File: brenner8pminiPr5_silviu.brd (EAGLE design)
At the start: 82.5 x 43 mm, 39 parts, among them IC1 PIC18F2550SP, Q1 20 MHz, Q2 BC338-25, Q3 BC338-25, Q4 BC328-25, Q5 BC328-25, Q6 BF959, X2 USB-B-H

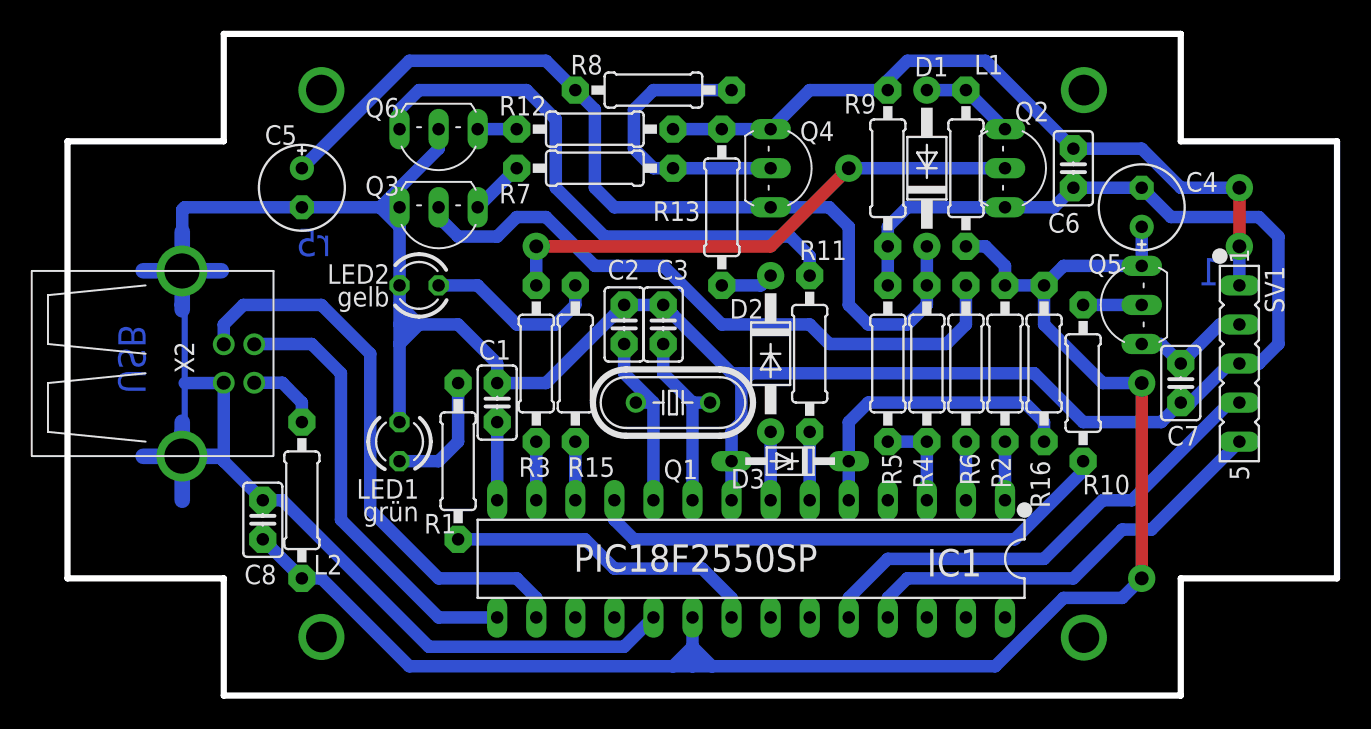
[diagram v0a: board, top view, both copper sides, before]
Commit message: Fixed DRC clearances and pad shapes
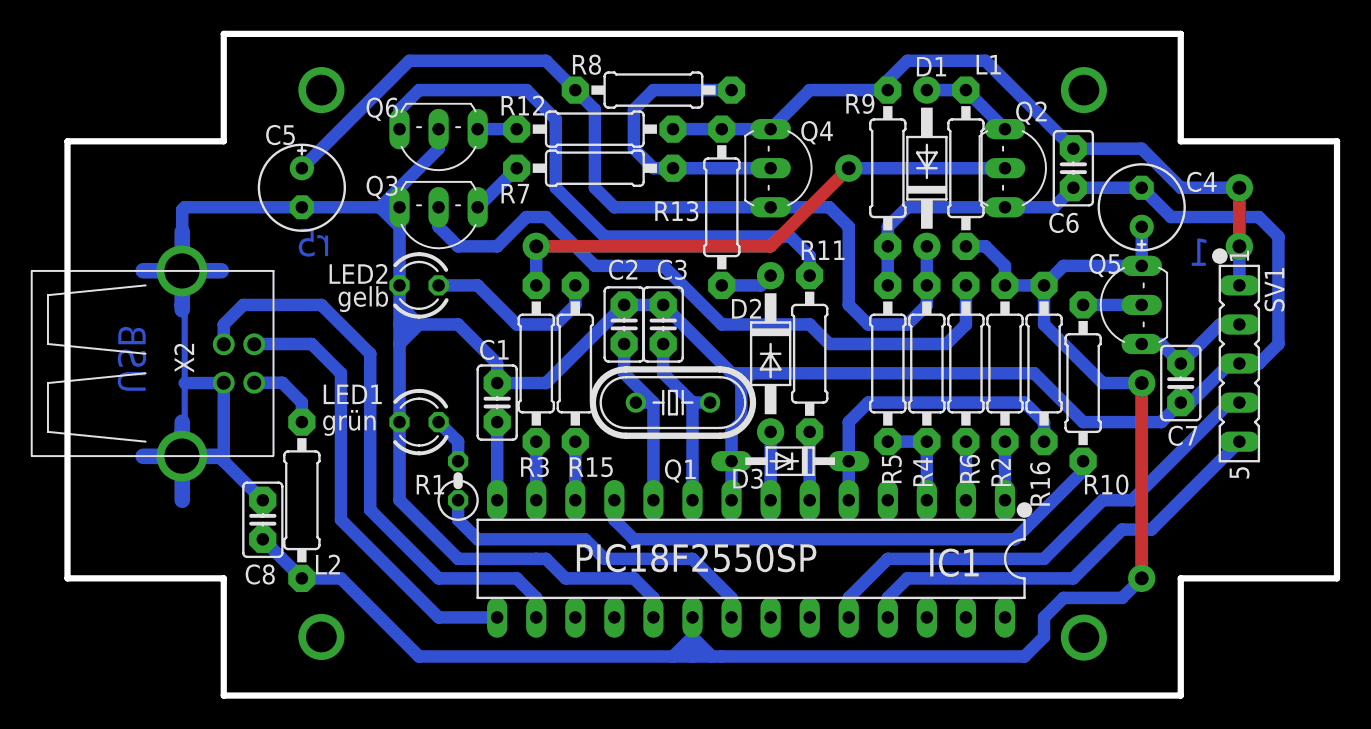
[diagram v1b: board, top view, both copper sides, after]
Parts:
- R1: device rcl:0207/10 -> rcl:0207/2V
- moved LED1 1.80 mm to (22.9, 16.5), turned to 180 degrees
- moved R1 1.27 mm to (25.4, 12.7)
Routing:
- net N$4: track 8.15 -> 3.07 mm
- net VSS: track 231.5 -> 226.8 mm
- net N$16: track 20.6 -> 22.4 mm
- net N$21: track 42.5 -> 43.4 mm

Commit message: Added silkscreen labels. Final DRC error fixes
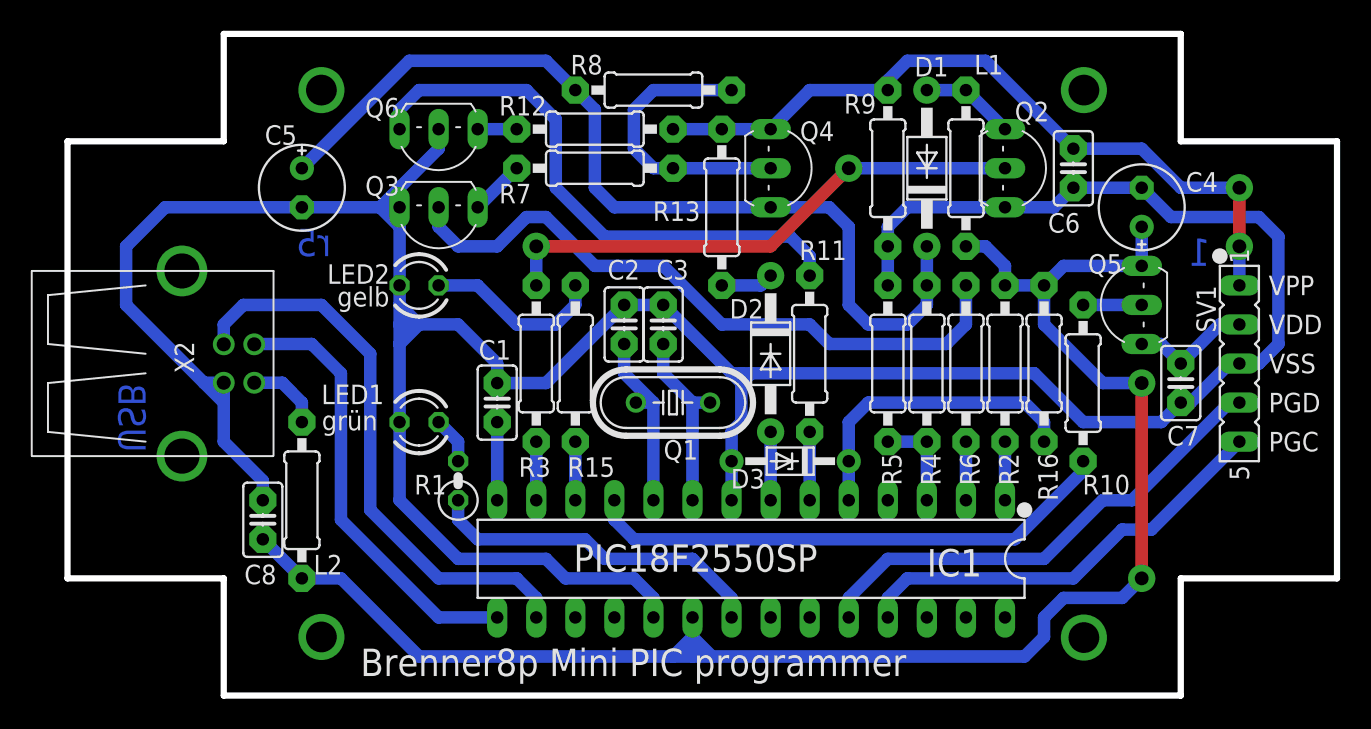
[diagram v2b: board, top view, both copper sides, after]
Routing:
- net VSS: track 226.8 -> 210.1 mm
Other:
- board text added: "Brenner8p Mini PIC programmer"
- board text added: "PGC"
- board text added: "PGD"
- board text added: "VDD"
- board text added: "VPP"
- board text added: "VSS"
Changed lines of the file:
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@@
 <wire x1="82.55" y1="34.77" x2="72.39" y2="34.77" width="0.4064" layer="20"/>
 <wire x1="82.55" y1="6.35" x2="72.39" y2="6.35" width="0.4064" layer="20"/>
-<text x="5.08" y="22.86" size="1.778" layer="16" font="vector" ratio="15" rot="MR270">USB</text>
+<text x="5.08" y="19.05" size="1.778" layer="16" font="vector" ratio="15" rot="MR270">USB</text>
 <text x="17.145" y="27.305" size="1.778" layer="16" font="vector" ratio="15" rot="MR0">r5</text>
 <text x="74.295" y="26.67" size="1.778" layer="16" font="vector" ratio="15" rot="MR0">1</text>
 <circle x="74.93" y="27.305" radius="0.508" width="0" layer="21"/>
 <circle x="62.23" y="10.795" radius="0.508" width="0" layer="21"/>
+<text x="19.05" y="0" size="1.778" layer="21">Brenner8p Mini PIC programmer</text>
+<text x="78.105" y="24.765" size="1.27" layer="21" ratio="10">VPP</text>
+<text x="78.105" y="22.225" size="1.27" layer="21" ratio="10">VDD</text>
+<text x="78.105" y="19.685" size="1.27" layer="21" ratio="10">VSS</text>
+<text x="78.105" y="17.145" size="1.27" layer="21" ratio="10">PGD</text>
+<text x="78.105" y="14.605" size="1.27" layer="21" ratio="10">PGC</text>
 </plain>
 <attributes>
@@
 </element>
 <element name="Q1" library="crystal" package="HC49/S" value="20 MHz" x="39.37" y="17.78" smashed="yes">
-<attribute name="NAME" x="38.7604" y="12.8016" size="1.27" layer="25" ratio="10"/>
+<attribute name="NAME" x="38.7604" y="14.0716" size="1.27" layer="25" ratio="10"/>
 <attribute name="VALUE" x="36.83" y="13.7922" size="1.27" layer="27" ratio="10"/>
 </element>
@@
 </element>
 <element name="R2" library="rcl" package="0207/10" value="10 k" x="60.96" y="20.32" smashed="yes" rot="R90">
-<attribute name="NAME" x="61.341" y="12.192" size="1.27" layer="25" ratio="10" rot="R90"/>
+<attribute name="NAME" x="60.579" y="14.478" size="1.27" layer="25" ratio="10" rot="R270"/>
 <attribute name="VALUE" x="61.595" y="18.0594" size="1.27" layer="27" ratio="10" rot="R90"/>
 </element>
@@
 </element>
 <element name="R4" library="rcl" package="0207/10" value="4k7" x="55.88" y="20.32" smashed="yes" rot="R90">
-<attribute name="NAME" x="56.261" y="12.192" size="1.27" layer="25" ratio="10" rot="R90"/>
+<attribute name="NAME" x="55.499" y="14.478" size="1.27" layer="25" ratio="10" rot="R270"/>
 <attribute name="VALUE" x="56.515" y="19.3294" size="1.27" layer="27" ratio="10" rot="R90"/>
 </element>
@@
 <attribute name="VALUE" x="11.049" y="8.001" size="1.27" layer="27" ratio="10" rot="R90"/>
 </element>
-<element name="SV1" library="con-lsta" package="FE05-1" value="ICSP" x="76.2" y="20.32" rot="R270"/>
+<element name="SV1" library="con-lsta" package="FE05-1" value="ICSP" x="76.2" y="20.32" smashed="yes" rot="R270">
+<attribute name="NAME" x="73.406" y="25.4" size="1.27" layer="25" ratio="10" rot="R270"/>
+<attribute name="VALUE" x="77.851" y="20.32" size="1.27" layer="27" ratio="10" rot="R270"/>
+</element>
 <element name="R15" library="rcl" package="0207/10" value="1 k" x="33.02" y="20.32" smashed="yes" rot="R270">
 <attribute name="NAME" x="32.512" y="12.954" size="1.27" layer="25" ratio="10"/>
@@
 </element>
 <element name="R16" library="rcl" package="0207/10" value="330" x="63.5" y="20.32" smashed="yes" rot="R90">
-<attribute name="NAME" x="63.881" y="10.922" size="1.27" layer="25" ratio="10" rot="R90"/>
+<attribute name="NAME" x="63.119" y="14.478" size="1.27" layer="25" ratio="10" rot="R270"/>
 <attribute name="VALUE" x="64.135" y="18.6944" size="1.27" layer="27" ratio="10" rot="R90"/>
 </element>
@@
 <wire x1="68.58" y1="5.08" x2="69.85" y2="6.35" width="0.8128" layer="16"/>
 <wire x1="40.64" y1="1.27" x2="41.91" y2="1.27" width="0.8128" layer="16"/>
-<wire x1="41.91" y1="1.27" x2="42.545" y2="1.27" width="0.8128" layer="16"/>
-<wire x1="42.545" y1="1.27" x2="62.23" y2="1.27" width="0.8128" layer="16"/>
+<wire x1="41.91" y1="1.27" x2="62.23" y2="1.27" width="0.8128" layer="16"/>
 <wire x1="62.23" y1="1.27" x2="63.5" y2="2.54" width="0.8128" layer="16"/>
 <wire x1="63.5" y1="2.54" x2="63.5" y2="3.81" width="0.8128" layer="16"/>
@@
 <wire x1="67.31" y1="19.05" x2="63.5" y2="22.86" width="0.8128" layer="16"/>
 <wire x1="63.5" y1="22.86" x2="63.5" y2="25.4" width="0.8128" layer="16"/>
-<wire x1="40.64" y1="1.27" x2="40.64" y2="1.905" width="0.8128" layer="16"/>
-<wire x1="40.64" y1="1.905" x2="40.64" y2="2.54" width="0.8128" layer="16"/>
+<wire x1="40.64" y1="1.27" x2="40.64" y2="2.54" width="0.8128" layer="16"/>
 <wire x1="40.64" y1="2.54" x2="40.64" y2="3.81" width="0.8128" layer="16"/>
 <wire x1="22.86" y1="1.27" x2="39.37" y2="1.27" width="0.8128" layer="16"/>
@@
 <wire x1="77.47" y1="29.845" x2="71.755" y2="29.845" width="0.8128" layer="16"/>
 <wire x1="27.94" y1="19.05" x2="31.115" y2="19.05" width="0.8128" layer="16"/>
-<wire x1="10.16" y1="19.05" x2="10.16" y2="19.07" width="0.8128" layer="16"/>
-<wire x1="10.16" y1="13.97" x2="12.7" y2="11.43" width="0.8128" layer="16"/>
-<wire x1="10.16" y1="19.05" x2="10.16" y2="13.97" width="0.8128" layer="16"/>
-<wire x1="7.62" y1="19.05" x2="10.16" y2="19.05" width="0.8128" layer="16"/>
-<wire x1="7.62" y1="30.48" x2="15.24" y2="30.48" width="0.8128" layer="16"/>
 <wire x1="15.24" y1="30.48" x2="20.32" y2="30.48" width="0.8128" layer="16"/>
 <wire x1="20.32" y1="30.48" x2="21.59" y2="30.48" width="0.8128" layer="16"/>
-<wire x1="7.4612" y1="24.13" x2="7.4612" y2="23.8125" width="1.016" layer="16"/>
-<wire x1="7.4612" y1="24.13" x2="7.4612" y2="28.8925" width="1.016" layer="16"/>
-<wire x1="7.62" y1="26.3525" x2="4.9213" y2="26.3525" width="1.016" layer="16"/>
-<wire x1="7.62" y1="26.3525" x2="10.0013" y2="26.3525" width="1.016" layer="16"/>
-<wire x1="10.0013" y1="14.2875" x2="4.9213" y2="14.2875" width="1.016" layer="16"/>
-<wire x1="7.4612" y1="11.43" x2="7.4612" y2="15.875" width="1.016" layer="16"/>
-<wire x1="7.4612" y1="15.875" x2="7.4612" y2="16.51" width="1.016" layer="16"/>
 <wire x1="43.18" y1="19.685" x2="43.815" y2="19.685" width="0.8128" layer="16"/>
 <wire x1="43.815" y1="19.685" x2="44.45" y2="19.685" width="0.8128" layer="16"/>
@@
 <wire x1="71.12" y1="16.51" x2="72.39" y2="17.78" width="0.8128" layer="16"/>
 <wire x1="36.195" y1="24.13" x2="38.735" y2="24.13" width="0.8128" layer="16"/>
-<wire x1="35.56" y1="23.495" x2="36.195" y2="24.13" width="0.8128" layer="16"/>
-<wire x1="31.115" y1="19.05" x2="35.56" y2="23.495" width="0.8128" layer="16"/>
-<wire x1="38.735" y1="24.13" x2="39.37" y2="23.495" width="0.8128" layer="16"/>
-<wire x1="39.37" y1="23.495" x2="43.18" y2="19.685" width="0.8128" layer="16"/>
-<wire x1="7.4612" y1="28.8925" x2="7.4612" y2="30.3212" width="0.8128" layer="16"/>
-<wire x1="7.4612" y1="30.3212" x2="7.62" y2="30.48" width="0.8128" layer="16"/>
-<wire x1="10.0013" y1="14.1287" x2="10.0013" y2="14.2875" width="0.8128" layer="16"/>
-<wire x1="10.16" y1="13.97" x2="10.0013" y2="14.1287" width="0.8128" layer="16"/>
-<wire x1="7.62" y1="24.13" x2="7.4612" y2="24.13" width="0.4064" layer="16"/>
-<wire x1="7.62" y1="19.05" x2="7.62" y2="24.13" width="0.4064" layer="16"/>
-<wire x1="7.62" y1="24.13" x2="7.62" y2="26.3525" width="0.4064" layer="16"/>
-<wire x1="7.4612" y1="15.875" x2="7.62" y2="15.875" width="0.4064" layer="16"/>
-<wire x1="7.62" y1="15.875" x2="7.62" y2="19.05" width="0.4064" layer="16"/>
+<wire x1="31.115" y1="19.05" x2="36.195" y2="24.13" width="0.8128" layer="16"/>
+<wire x1="38.735" y1="24.13" x2="43.18" y2="19.685" width="0.8128" layer="16"/>
 <wire x1="21.59" y1="31.75" x2="24.13" y2="34.29" width="0.8128" layer="16"/>
 <wire x1="21.59" y1="30.48" x2="21.59" y2="31.75" width="0.8128" layer="16"/>
@@
 <wire x1="36.83" y1="6.35" x2="32.385" y2="6.35" width="0.8128" layer="16"/>
 <wire x1="32.385" y1="6.35" x2="31.115" y2="7.62" width="0.8128" layer="16"/>
-<wire x1="31.115" y1="7.62" x2="30.48" y2="7.62" width="0.8128" layer="16"/>
-<wire x1="30.48" y1="7.62" x2="25.4" y2="7.62" width="0.8128" layer="16"/>
+<wire x1="31.115" y1="7.62" x2="25.4" y2="7.62" width="0.8128" layer="16"/>
 <wire x1="25.4" y1="7.62" x2="21.59" y2="11.43" width="0.8128" layer="16"/>
 <wire x1="21.59" y1="11.43" x2="21.59" y2="16.51" width="0.8128" layer="16"/>
+<wire x1="12.7" y1="11.43" x2="12.7" y2="12.7" width="0.8128" layer="16"/>
+<wire x1="12.7" y1="12.7" x2="10.16" y2="15.24" width="0.8128" layer="16"/>
+<wire x1="10.16" y1="19.07" x2="8.87" y2="19.07" width="0.8128" layer="16"/>
+<wire x1="8.87" y1="19.07" x2="3.81" y2="24.13" width="0.8128" layer="16"/>
+<wire x1="3.81" y1="24.13" x2="3.81" y2="27.94" width="0.8128" layer="16"/>
+<wire x1="3.81" y1="27.94" x2="6.35" y2="30.48" width="0.8128" layer="16"/>
+<wire x1="6.35" y1="30.48" x2="15.24" y2="30.48" width="0.8128" layer="16"/>
+<wire x1="10.16" y1="19.07" x2="10.16" y2="17.78" width="0.8128" layer="16"/>
+<wire x1="10.16" y1="17.78" x2="10.16" y2="15.24" width="0.8128" layer="16"/>
+<wire x1="8.89" y1="19.05" x2="10.16" y2="17.78" width="0.8128" layer="16"/>
 </signal>
 <signal name="N$29">
